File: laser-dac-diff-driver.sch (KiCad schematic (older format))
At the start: 16 parts, among them P101 CONN_2, P102 CONN_3X2, P103 CONN_6X2, U101 AD5689RARUZ, U102 74HC04

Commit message: Fixed decoupling on 78HC04, sorted out component positions
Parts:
- removed C104: C, symbol C
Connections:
- net +5VD: no longer C102.1, C103.1
- net AGND: now also P103.9; no longer P103.3 (P3)
- net MOD_VCC: now also C102.1, C103.1
- net powersupply/+Vin: now also P103.11; no longer P103.9
- net ~LDAC: now also P103.3 (P3); no longer P103.11
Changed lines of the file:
@@
 LIBS:valves
 LIBS:ad5689raruz
+LIBS:Symbols_DCDC-ACDC-Converter_RevC_20Jul2012
 LIBS:op470
-LIBS:arduino_shieldsNCL
-LIBS:Symbols_DCDC-ACDC-Converter_RevC_20Jul2012
-LIBS:laserdac-cache
+LIBS:laser-dac-diff-driver-cache
 EELAYER 24 0
 EELAYER END
@@
 	750  4000 750  6500
 Wire Wire Line
-	800  4100 800  6400
-Wire Wire Line
 	1700 2900 4450 2900
 Connection ~ 10250 5150
@@
 $EndComp
 Wire Wire Line
-	1800 4300 1800 4200
-Wire Wire Line
-	1800 4200 1900 4200
-Wire Wire Line
-	800  4100 1900 4100
-Wire Wire Line
-	750  4000 1900 4000
+	1800 4300 1800 3800
 Wire Wire Line
 	1700 2900 1700 3700
@@
 $EndComp
 $Comp
-L C C104
-U 1 1 52F9E40F
-P 7500 950
-F 0 "C104" H 7500 1050 40  0000 L CNN
-F 1 "C" H 7506 865 40  0000 L CNN
-F 2 "" H 7538 800 30  0000 C CNN
-F 3 "" H 7500 950 60  0000 C CNN
-	1    7500 950
-	1    0    0    -1
-$EndComp
-$Comp
-L +5VD #PWR019
-U 1 1 52F9E4CE
-P 6900 650
-F 0 "#PWR019" H 6900 600 20  0001 C CNN
-F 1 "+5VD" H 6900 750 30  0000 C CNN
-F 2 "" H 6900 650 60  0000 C CNN
-F 3 "" H 6900 650 60  0000 C CNN
-	1    6900 650
-	1    0    0    -1
-$EndComp
-$Comp
-L AGND #PWR020
+L AGND #PWR019
 U 1 1 52F9E4D9
 P 6900 1250
-F 0 "#PWR020" H 6900 1250 40  0001 C CNN
+F 0 "#PWR019" H 6900 1250 40  0001 C CNN
 F 1 "AGND" H 6900 1180 50  0000 C CNN
 F 2 "" H 6900 1250 60  0000 C CNN
@@
 $EndComp
 Wire Wire Line
-	6900 750  6900 650
-Wire Wire Line
-	7500 750  7500 700
-Wire Wire Line
-	7500 700  6900 700
+	6900 650  6900 750
+Wire Wire Line
+	7500 700  7500 750
+Wire Wire Line
+	6700 700  7500 700
 Connection ~ 6900 700
 Wire Wire Line
@@
 Connection ~ 6900 1200
 $Comp
-L DGND #PWR021
+L DGND #PWR020
 U 1 1 52F9FCBF
-P 1800 3850
-F 0 "#PWR021" H 1800 3850 40  0001 C CNN
-F 1 "DGND" H 1800 3780 40  0000 C CNN
-F 2 "" H 1800 3850 60  0000 C CNN
-F 3 "" H 1800 3850 60  0000 C CNN
-	1    1800 3850
-	1    0    0    -1
-$EndComp
-Wire Wire Line
-	1900 3800 1800 3800
-Wire Wire Line
-	1800 3800 1800 3850
+P 1700 4150
+F 0 "#PWR020" H 1700 4150 40  0001 C CNN
+F 1 "DGND" H 1700 4080 40  0000 C CNN
+F 2 "" H 1700 4150 60  0000 C CNN
+F 3 "" H 1700 4150 60  0000 C CNN
+	1    1700 4150
+	1    0    0    -1
+$EndComp
 Wire Wire Line
 	3550 3450 4450 3450
@@
 	4450 2900 4450 3600
 $Comp
-L +3.3VDAC #PWR022
+L +3.3VDAC #PWR021
 U 1 1 52FA10E9
 P 5900 1550
-F 0 "#PWR022" H 5900 1670 20  0001 C CNN
+F 0 "#PWR021" H 5900 1670 20  0001 C CNN
 F 1 "+3.3VDAC" H 5900 1640 30  0000 C CNN
 F 2 "" H 5900 1550 60  0000 C CNN
@@
 Connection ~ 6900 1650
 $Comp
-L +3.3VDAC #PWR023
+L +3.3VDAC #PWR022
 U 1 1 52FA287E
 P 2950 2850
-F 0 "#PWR023" H 2950 2970 20  0001 C CNN
+F 0 "#PWR022" H 2950 2970 20  0001 C CNN
 F 1 "+3.3VDAC" H 2950 2940 30  0000 C CNN
 F 2 "" H 2950 2850 60  0000 C CNN
@@
 Text Label 6750 1450 0    60   ~ 0
 MOD_VCC
+Wire Wire Line
+	1900 4200 800  4200
+Wire Wire Line
+	800  4200 800  6400
+Wire Wire Line
+	1800 3800 1900 3800
+Wire Wire Line
+	1900 4100 1700 4100
+Wire Wire Line
+	1700 4100 1700 4150
+Wire Wire Line
+	1900 4000 750  4000
+Wire Wire Line
+	6700 1450 6700 700
+Connection ~ 6700 1450
 $EndSCHEMATC

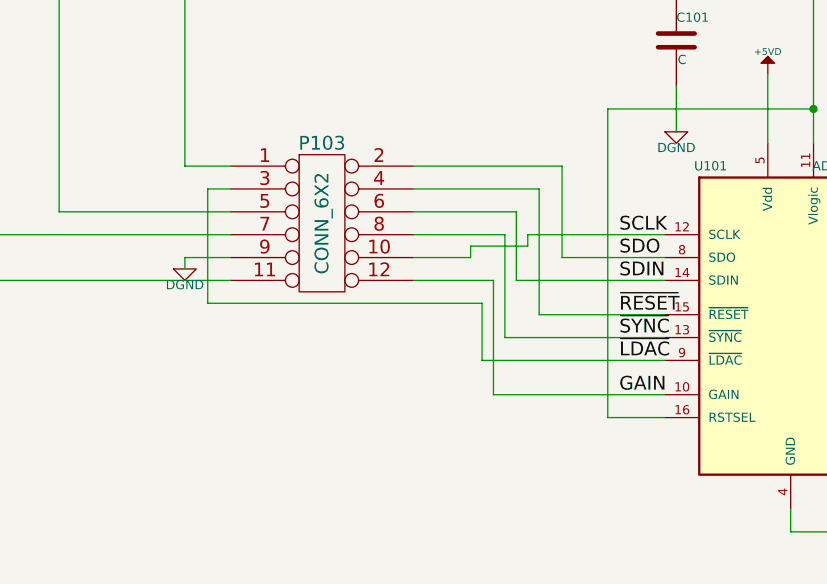
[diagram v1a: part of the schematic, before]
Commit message: Added extra small decoupling for reference. Pin-swapped and fixed pin numbers on digital input.
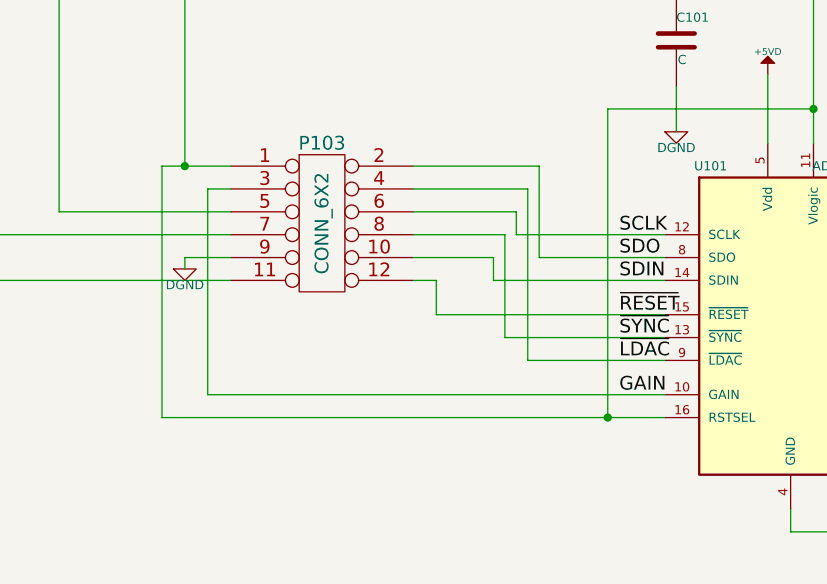
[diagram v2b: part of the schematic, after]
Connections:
- net GAIN: now also P103.3 (P3); no longer P103.12
- net SCLK: now also P103.6 (P6); no longer P103.10
- net SDIN: now also P103.10; no longer P103.6 (P6)
- net ~LDAC: now also P103.4 (P4); no longer P103.3 (P3)
- net ~RESET: now also P103.12; no longer P103.4 (P4)
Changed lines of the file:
@@
 $EndComp
-Wire Wire Line
-	3350 3700 2700 3700
 Wire Wire Line
 	750  4000 750  6500
@@
 	4350 5200 4350 5300
 Wire Wire Line
-	3350 4100 3800 4100
-Wire Wire Line
-	3350 3700 3350 4100
-Wire Wire Line
 	6300 5700 7850 5700
 Wire Wire Line
@@
 	3550 4800 3550 3450
 Wire Wire Line
-	3800 4800 3550 4800
+	1600 4800 3800 4800
 Wire Wire Line
 	4250 3300 4250 3600
@@
 Wire Wire Line
 	800  6400 1350 6400
-Wire Wire Line
-	3800 4550 3000 4550
-Wire Wire Line
-	3000 4550 3000 4300
-Wire Wire Line
-	3000 4300 1800 4300
-Wire Wire Line
-	3800 4700 3050 4700
-Wire Wire Line
-	3050 4700 3050 4200
-Wire Wire Line
-	3050 4200 2700 4200
-Wire Wire Line
-	2950 4100 2700 4100
-Wire Wire Line
-	3800 4450 3100 4450
-Wire Wire Line
-	3100 4450 3100 4000
-Wire Wire Line
-	3100 4000 2700 4000
-Wire Wire Line
-	3800 4000 3200 4000
-Wire Wire Line
-	3200 4000 3200 4050
-Wire Wire Line
-	3200 4050 2950 4050
-Wire Wire Line
-	2950 4050 2950 4100
-Wire Wire Line
-	3800 4200 3150 4200
-Wire Wire Line
-	3150 4200 3150 3900
-Wire Wire Line
-	3150 3900 2700 3900
-Wire Wire Line
-	3800 4350 3250 4350
-Wire Wire Line
-	3250 4350 3250 3800
-Wire Wire Line
-	3250 3800 2700 3800
 Wire Wire Line
 	3500 5600 3500 7150
@@
 $EndComp
 Wire Wire Line
-	1800 4300 1800 3800
-Wire Wire Line
 	1700 2900 1700 3700
 Wire Wire Line
-	1700 3700 1900 3700
+	1600 3700 1900 3700
 Wire Wire Line
 	1900 3900 1150 3900
@@
 	800  4200 800  6400
 Wire Wire Line
-	1800 3800 1900 3800
-Wire Wire Line
 	1900 4100 1700 4100
 Wire Wire Line
@@
 	6700 1450 6700 700
 Connection ~ 6700 1450
+Wire Wire Line
+	3800 4550 3200 4550
+Wire Wire Line
+	3800 4700 1800 4700
+Wire Wire Line
+	1800 4700 1800 3800
+Wire Wire Line
+	1800 3800 1900 3800
+Wire Wire Line
+	1600 4800 1600 3700
+Connection ~ 1700 3700
+Connection ~ 3550 4800
+Wire Wire Line
+	3200 4550 3200 3800
+Wire Wire Line
+	3200 3800 2700 3800
+Wire Wire Line
+	3800 4100 3250 4100
+Wire Wire Line
+	3250 4100 3250 3700
+Wire Wire Line
+	3250 3700 2700 3700
+Wire Wire Line
+	3800 4000 3150 4000
+Wire Wire Line
+	3150 4000 3150 3900
+Wire Wire Line
+	3150 3900 2700 3900
+Wire Wire Line
+	3800 4200 3050 4200
+Wire Wire Line
+	3050 4200 3050 4100
+Wire Wire Line
+	3050 4100 2700 4100
+Wire Wire Line
+	3800 4450 3100 4450
+Wire Wire Line
+	3100 4450 3100 4000
+Wire Wire Line
+	3100 4000 2700 4000
+Wire Wire Line
+	3800 4350 2800 4350
+Wire Wire Line
+	2800 4350 2800 4200
+Wire Wire Line
+	2800 4200 2700 4200
 $EndSCHEMATC

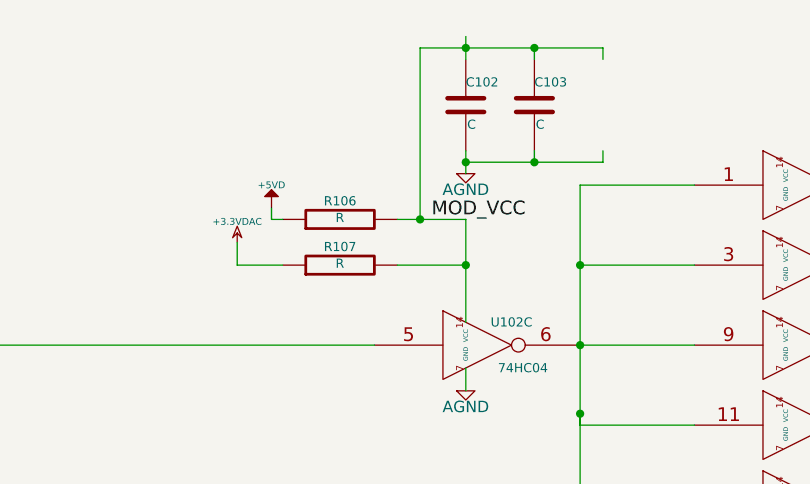
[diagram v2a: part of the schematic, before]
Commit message: A few autorouter attempts and a new board layout (component positions). Removed voltage selector for MOD driver, 5V only now.
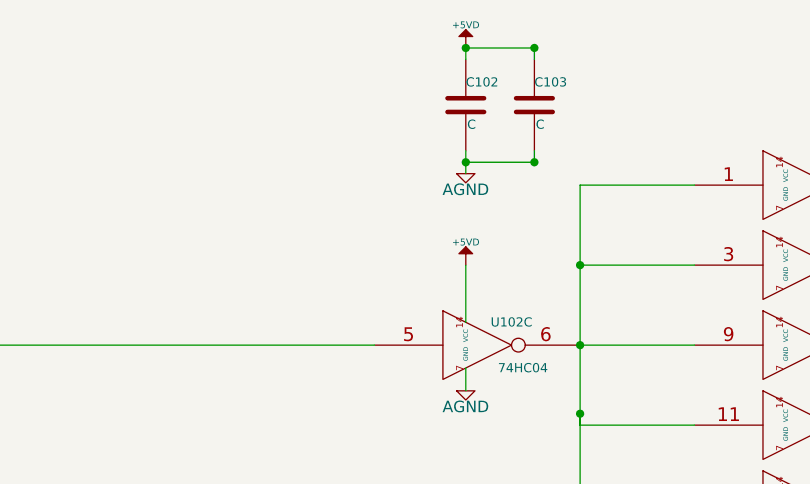
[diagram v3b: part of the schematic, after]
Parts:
- removed R106, R107: R, symbol R
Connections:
- net MOD_VCC is gone; now on net +5VD: C102.1, C103.1, U102.14 (VCC)
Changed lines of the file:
@@
 L +5VD #PWR017
 U 1 1 52F9D2EA
-P 6050 1400
-F 0 "#PWR017" H 6050 1350 20  0001 C CNN
-F 1 "+5VD" H 6050 1500 30  0000 C CNN
-F 2 "" H 6050 1400 60  0000 C CNN
-F 3 "" H 6050 1400 60  0000 C CNN
-	1    6050 1400
+P 6900 1650
+F 0 "#PWR017" H 6900 1600 20  0001 C CNN
+F 1 "+5VD" H 6900 1750 30  0000 C CNN
+F 2 "" H 6900 1650 60  0000 C CNN
+F 3 "" H 6900 1650 60  0000 C CNN
+	1    6900 1650
 	1    0    0    -1
 $EndComp
@@
 	1    0    0    -1
 $EndComp
-Wire Wire Line
-	6900 650  6900 750
-Wire Wire Line
-	7500 700  7500 750
-Wire Wire Line
-	6700 700  7500 700
 Connection ~ 6900 700
 Wire Wire Line
-	7200 750  7200 700
+	7200 700  7200 750
 Connection ~ 7200 700
-Wire Wire Line
-	7500 1200 7500 1150
-Wire Wire Line
-	6900 1200 7500 1200
 Wire Wire Line
 	7200 1200 7200 1150
@@
 Wire Wire Line
 	4450 2900 4450 3600
-$Comp
-L +3.3VDAC #PWR021
-U 1 1 52FA10E9
-P 5900 1550
-F 0 "#PWR021" H 5900 1670 20  0001 C CNN
-F 1 "+3.3VDAC" H 5900 1640 30  0000 C CNN
-F 2 "" H 5900 1550 60  0000 C CNN
-F 3 "" H 5900 1550 60  0000 C CNN
-	1    5900 1550
-	1    0    0    -1
-$EndComp
 Wire Wire Line
 	2950 2850 2950 2900
 Connection ~ 2950 2900
 $Comp
-L R R107
-U 1 1 52FA17BC
-P 6350 1650
-F 0 "R107" V 6430 1650 40  0000 C CNN
-F 1 "R" V 6357 1651 40  0000 C CNN
-F 2 "" V 6280 1650 30  0000 C CNN
-F 3 "" H 6350 1650 30  0000 C CNN
-	1    6350 1650
-	0    -1   -1   0
-$EndComp
-$Comp
-L R R106
-U 1 1 52FA187B
-P 6350 1450
-F 0 "R106" V 6430 1450 40  0000 C CNN
-F 1 "R" V 6357 1451 40  0000 C CNN
-F 2 "" V 6280 1450 30  0000 C CNN
-F 3 "" H 6350 1450 30  0000 C CNN
-	1    6350 1450
-	0    -1   -1   0
-$EndComp
-Wire Wire Line
-	6050 1400 6050 1450
-Wire Wire Line
-	6050 1450 6100 1450
-Wire Wire Line
-	5900 1550 5900 1650
-Wire Wire Line
-	5900 1650 6100 1650
-Wire Wire Line
-	6600 1650 6900 1650
-Wire Wire Line
-	6900 1450 6900 1900
-Wire Wire Line
-	6600 1450 6900 1450
-Connection ~ 6900 1650
-$Comp
-L +3.3VDAC #PWR022
+L +3.3VDAC #PWR021
 U 1 1 52FA287E
 P 2950 2850
-F 0 "#PWR022" H 2950 2970 20  0001 C CNN
+F 0 "#PWR021" H 2950 2970 20  0001 C CNN
 F 1 "+3.3VDAC" H 2950 2940 30  0000 C CNN
 F 2 "" H 2950 2850 60  0000 C CNN
@@
 Text Label 9600 1300 0    60   ~ 0
 MOD_OUT
-Text Label 6750 1450 0    60   ~ 0
-MOD_VCC
 Wire Wire Line
 	1900 4200 800  4200
@@
 Wire Wire Line
 	1900 4000 750  4000
-Wire Wire Line
-	6700 1450 6700 700
-Connection ~ 6700 1450
 Wire Wire Line
 	3800 4550 3200 4550
@@
 Wire Wire Line
 	2800 4200 2700 4200
+Wire Wire Line
+	6900 700  6900 750
+Wire Wire Line
+	6900 1200 7200 1200
+Wire Wire Line
+	6900 1900 6900 1650
+$Comp
+L +5VD #PWR022
+U 1 1 53152500
+P 6900 700
+F 0 "#PWR022" H 6900 650 20  0001 C CNN
+F 1 "+5VD" H 6900 800 30  0000 C CNN
+F 2 "" H 6900 700 60  0000 C CNN
+F 3 "" H 6900 700 60  0000 C CNN
+	1    6900 700
+	1    0    0    -1
+$EndComp
+Wire Wire Line
+	6900 700  7200 700
 $EndSCHEMATC

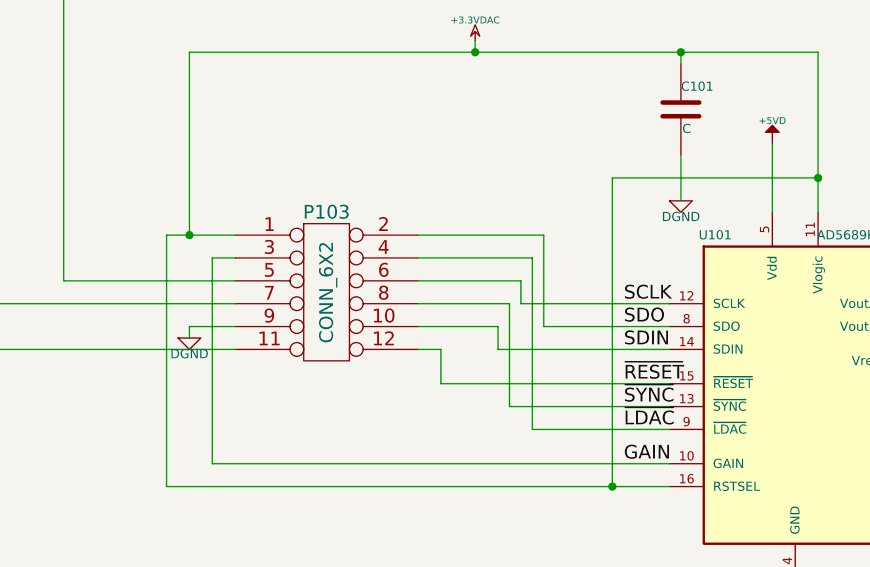
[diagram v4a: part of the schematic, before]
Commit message: SENT TO FAB - also added LC filter to power from 5V to dac, copper pours for Reg heatsinks and missing resistors
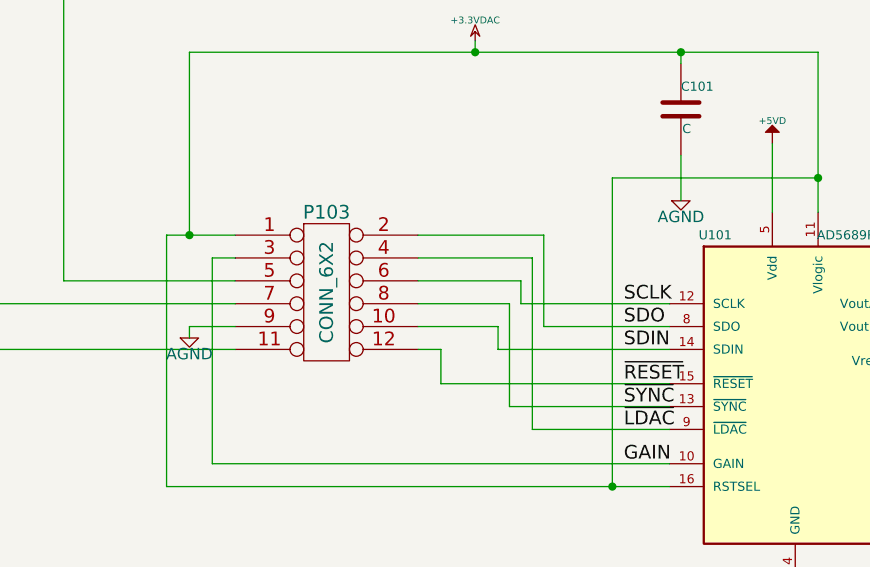
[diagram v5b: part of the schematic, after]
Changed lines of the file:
@@
 EESchema Schematic File Version 2
+LIBS:LM317_HS
 LIBS:74hct04
 LIBS:power
@@
 LIBS:op470
 LIBS:laser-dac-diff-driver-cache
-EELAYER 27 0
+EELAYER 24 0
 EELAYER END
 $Descr A4 11693 8268
@@
 $EndComp
 $Comp
-L DGND #PWR07
-U 1 1 52F5B8DB
-P 3850 3550
-F 0 "#PWR07" H 3850 3550 40  0001 C CNN
-F 1 "DGND" H 3850 3480 40  0000 C CNN
-F 2 "" H 3850 3550 60  0000 C CNN
-F 3 "" H 3850 3550 60  0000 C CNN
-	1    3850 3550
-	1    0    0    -1
-$EndComp
-$Comp
-L VAA #PWR08
+L VAA #PWR07
 U 1 1 52F5C033
 P 7650 5250
-F 0 "#PWR08" H 7650 5310 30  0001 C CNN
+F 0 "#PWR07" H 7650 5310 30  0001 C CNN
 F 1 "VAA" H 7650 5360 30  0000 C CNN
 F 2 "" H 7650 5250 60  0000 C CNN
@@
 $EndComp
 $Comp
-L -VAA #PWR09
+L -VAA #PWR08
 U 1 1 52F5C047
 P 7650 5550
-F 0 "#PWR09" H 7650 5650 20  0001 C CNN
+F 0 "#PWR08" H 7650 5650 20  0001 C CNN
 F 1 "-VAA" H 7650 5650 30  0000 C CNN
 F 2 "" H 7650 5550 60  0000 C CNN
@@
 $EndComp
 $Comp
-L AGND #PWR010
+L AGND #PWR09
 U 1 1 52F5C05B
 P 7450 5450
-F 0 "#PWR010" H 7450 5450 40  0001 C CNN
+F 0 "#PWR09" H 7450 5450 40  0001 C CNN
 F 1 "AGND" H 7450 5380 50  0000 C CNN
 F 2 "" H 7450 5450 60  0000 C CNN
@@
 $EndComp
 $Comp
-L VAA #PWR011
+L VAA #PWR010
 U 1 1 52F5CB91
 P 7650 3650
-F 0 "#PWR011" H 7650 3710 30  0001 C CNN
+F 0 "#PWR010" H 7650 3710 30  0001 C CNN
 F 1 "VAA" H 7650 3760 30  0000 C CNN
 F 2 "" H 7650 3650 60  0000 C CNN
@@
 $EndComp
 $Comp
-L -VAA #PWR012
+L -VAA #PWR011
 U 1 1 52F5CB97
 P 7650 3950
-F 0 "#PWR012" H 7650 4050 20  0001 C CNN
+F 0 "#PWR011" H 7650 4050 20  0001 C CNN
 F 1 "-VAA" H 7650 4050 30  0000 C CNN
 F 2 "" H 7650 3950 60  0000 C CNN
@@
 $EndComp
 $Comp
-L AGND #PWR013
+L AGND #PWR012
 U 1 1 52F5CB9D
 P 7450 3850
-F 0 "#PWR013" H 7450 3850 40  0001 C CNN
+F 0 "#PWR012" H 7450 3850 40  0001 C CNN
 F 1 "AGND" H 7450 3780 50  0000 C CNN
 F 2 "" H 7450 3850 60  0000 C CNN
@@
 $EndComp
 $Comp
-L AGND #PWR014
+L AGND #PWR013
 U 1 1 52F5ED00
 P 4750 5800
-F 0 "#PWR014" H 4750 5800 40  0001 C CNN
+F 0 "#PWR013" H 4750 5800 40  0001 C CNN
 F 1 "AGND" H 4750 5730 50  0000 C CNN
 F 2 "" H 4750 5800 60  0000 C CNN
@@
 $EndComp
 $Comp
-L AGND #PWR015
+L AGND #PWR014
 U 1 1 52F5F65C
 P 10250 5200
-F 0 "#PWR015" H 10250 5200 40  0001 C CNN
+F 0 "#PWR014" H 10250 5200 40  0001 C CNN
 F 1 "AGND" H 10250 5130 50  0000 C CNN
 F 2 "" H 10250 5200 60  0000 C CNN
@@
 	9800 1500 9800 1600
 $Comp
-L AGND #PWR016
+L AGND #PWR015
 U 1 1 52F992F9
 P 9800 1600
-F 0 "#PWR016" H 9800 1600 40  0001 C CNN
+F 0 "#PWR015" H 9800 1600 40  0001 C CNN
 F 1 "AGND" H 9800 1530 50  0000 C CNN
 F 2 "" H 9800 1600 60  0000 C CNN
@@
 	1150 2000 6500 2000
 $Comp
-L +5VD #PWR017
+L +5VD #PWR016
 U 1 1 52F9D2EA
 P 6900 1650
-F 0 "#PWR017" H 6900 1600 20  0001 C CNN
+F 0 "#PWR016" H 6900 1600 20  0001 C CNN
 F 1 "+5VD" H 6900 1750 30  0000 C CNN
 F 2 "" H 6900 1650 60  0000 C CNN
@@
 $EndComp
 $Comp
-L AGND #PWR018
+L AGND #PWR017
 U 1 1 52F9D829
 P 6900 2200
-F 0 "#PWR018" H 6900 2200 40  0001 C CNN
+F 0 "#PWR017" H 6900 2200 40  0001 C CNN
 F 1 "AGND" H 6900 2130 50  0000 C CNN
 F 2 "" H 6900 2200 60  0000 C CNN
@@
 $EndComp
 $Comp
-L AGND #PWR019
+L AGND #PWR018
 U 1 1 52F9E4D9
 P 6900 1250
-F 0 "#PWR019" H 6900 1250 40  0001 C CNN
+F 0 "#PWR018" H 6900 1250 40  0001 C CNN
 F 1 "AGND" H 6900 1180 50  0000 C CNN
 F 2 "" H 6900 1250 60  0000 C CNN
@@
 Connection ~ 7200 1200
 Connection ~ 6900 1200
-$Comp
-L DGND #PWR020
-U 1 1 52F9FCBF
-P 1700 4150
-F 0 "#PWR020" H 1700 4150 40  0001 C CNN
-F 1 "DGND" H 1700 4080 40  0000 C CNN
-F 2 "" H 1700 4150 60  0000 C CNN
-F 3 "" H 1700 4150 60  0000 C CNN
-	1    1700 4150
-	1    0    0    -1
-$EndComp
 Wire Wire Line
 	3550 3450 4450 3450
@@
 Connection ~ 2950 2900
 $Comp
-L +3.3VDAC #PWR021
+L +3.3VDAC #PWR019
 U 1 1 52FA287E
 P 2950 2850
-F 0 "#PWR021" H 2950 2970 20  0001 C CNN
+F 0 "#PWR019" H 2950 2970 20  0001 C CNN
 F 1 "+3.3VDAC" H 2950 2940 30  0000 C CNN
 F 2 "" H 2950 2850 60  0000 C CNN
@@
 	6900 1900 6900 1650
 $Comp
-L +5VD #PWR022
+L +5VD #PWR020
 U 1 1 53152500
 P 6900 700
-F 0 "#PWR022" H 6900 650 20  0001 C CNN
+F 0 "#PWR020" H 6900 650 20  0001 C CNN
 F 1 "+5VD" H 6900 800 30  0000 C CNN
 F 2 "" H 6900 700 60  0000 C CNN
@@
 Wire Wire Line
 	6900 700  7200 700
+$Comp
+L AGND #PWR021
+U 1 1 53178F03
+P 3850 3550
+F 0 "#PWR021" H 3850 3550 40  0001 C CNN
+F 1 "AGND" H 3850 3480 50  0000 C CNN
+F 2 "" H 3850 3550 60  0000 C CNN
+F 3 "" H 3850 3550 60  0000 C CNN
+	1    3850 3550
+	1    0    0    -1
+$EndComp
+$Comp
+L AGND #PWR022
+U 1 1 531790F7
+P 1700 4150
+F 0 "#PWR022" H 1700 4150 40  0001 C CNN
+F 1 "AGND" H 1700 4080 50  0000 C CNN
+F 2 "" H 1700 4150 60  0000 C CNN
+F 3 "" H 1700 4150 60  0000 C CNN
+	1    1700 4150
+	1    0    0    -1
+$EndComp
 $EndSCHEMATC
